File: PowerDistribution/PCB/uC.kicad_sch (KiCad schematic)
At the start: 11 parts, among them IC11 ESP32-S3-WROOM-1U-N8, J10 USB_C_Receptacle_USB2.0_16P, SW1 SW_Push, SW2 SW_Push, U2 USBLC6-2SC6

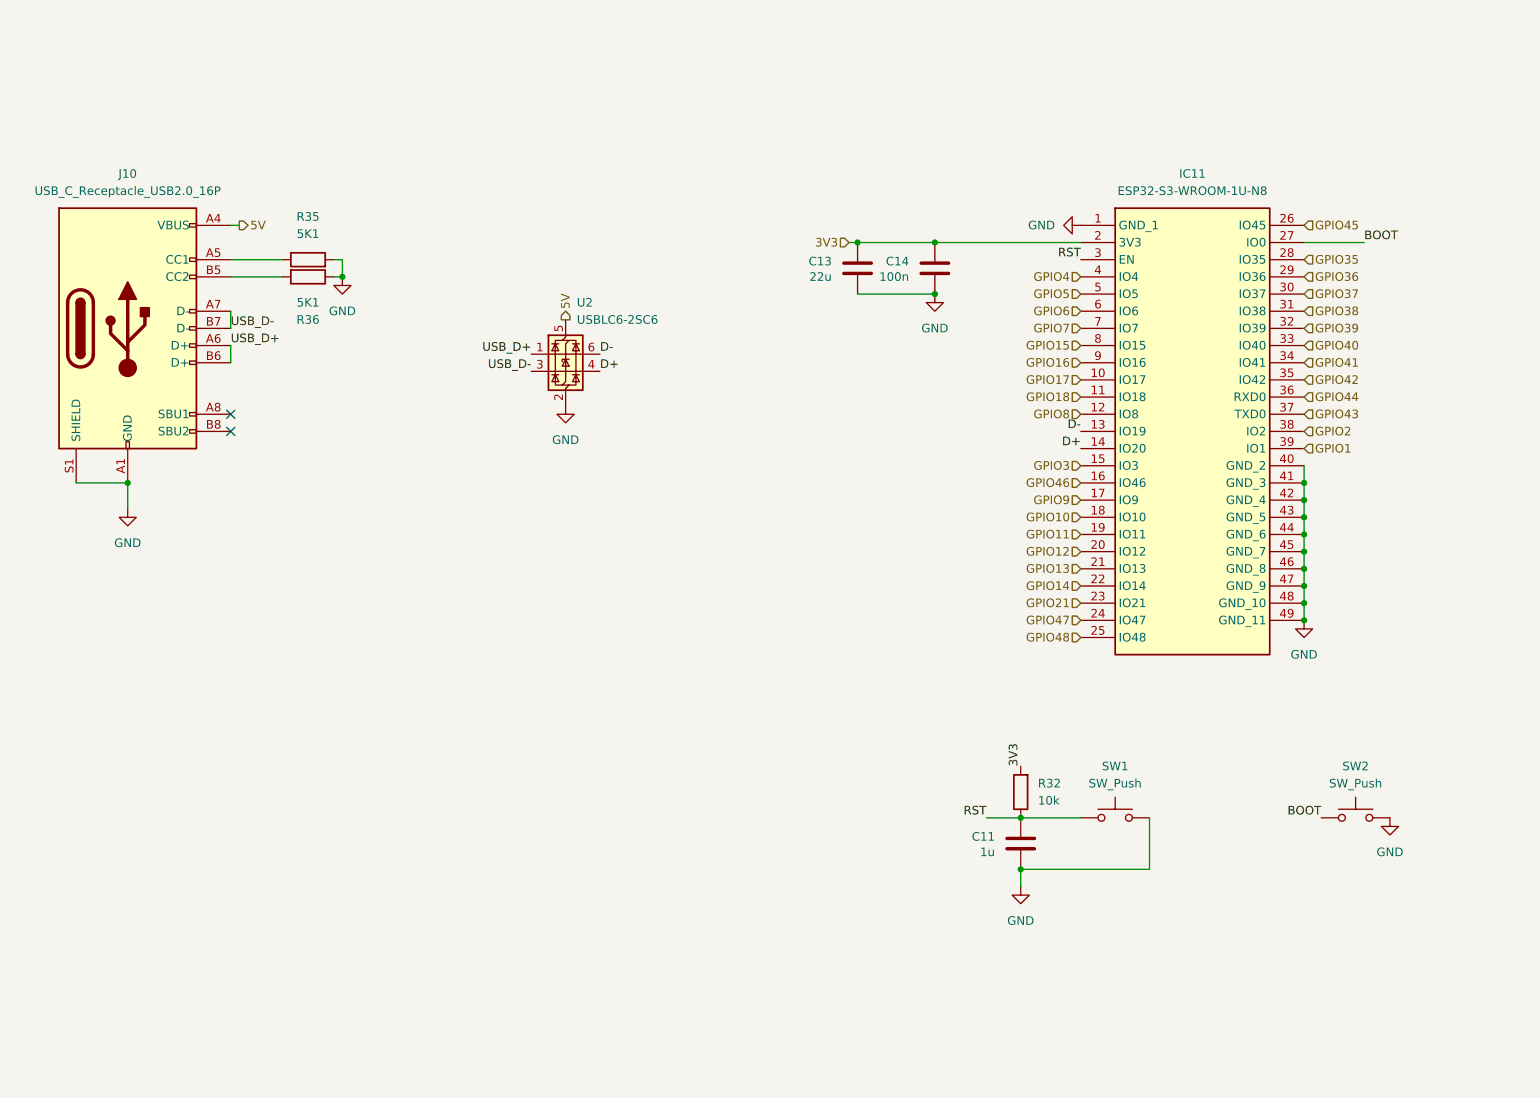
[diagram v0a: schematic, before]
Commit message: Adds PDB v2.0
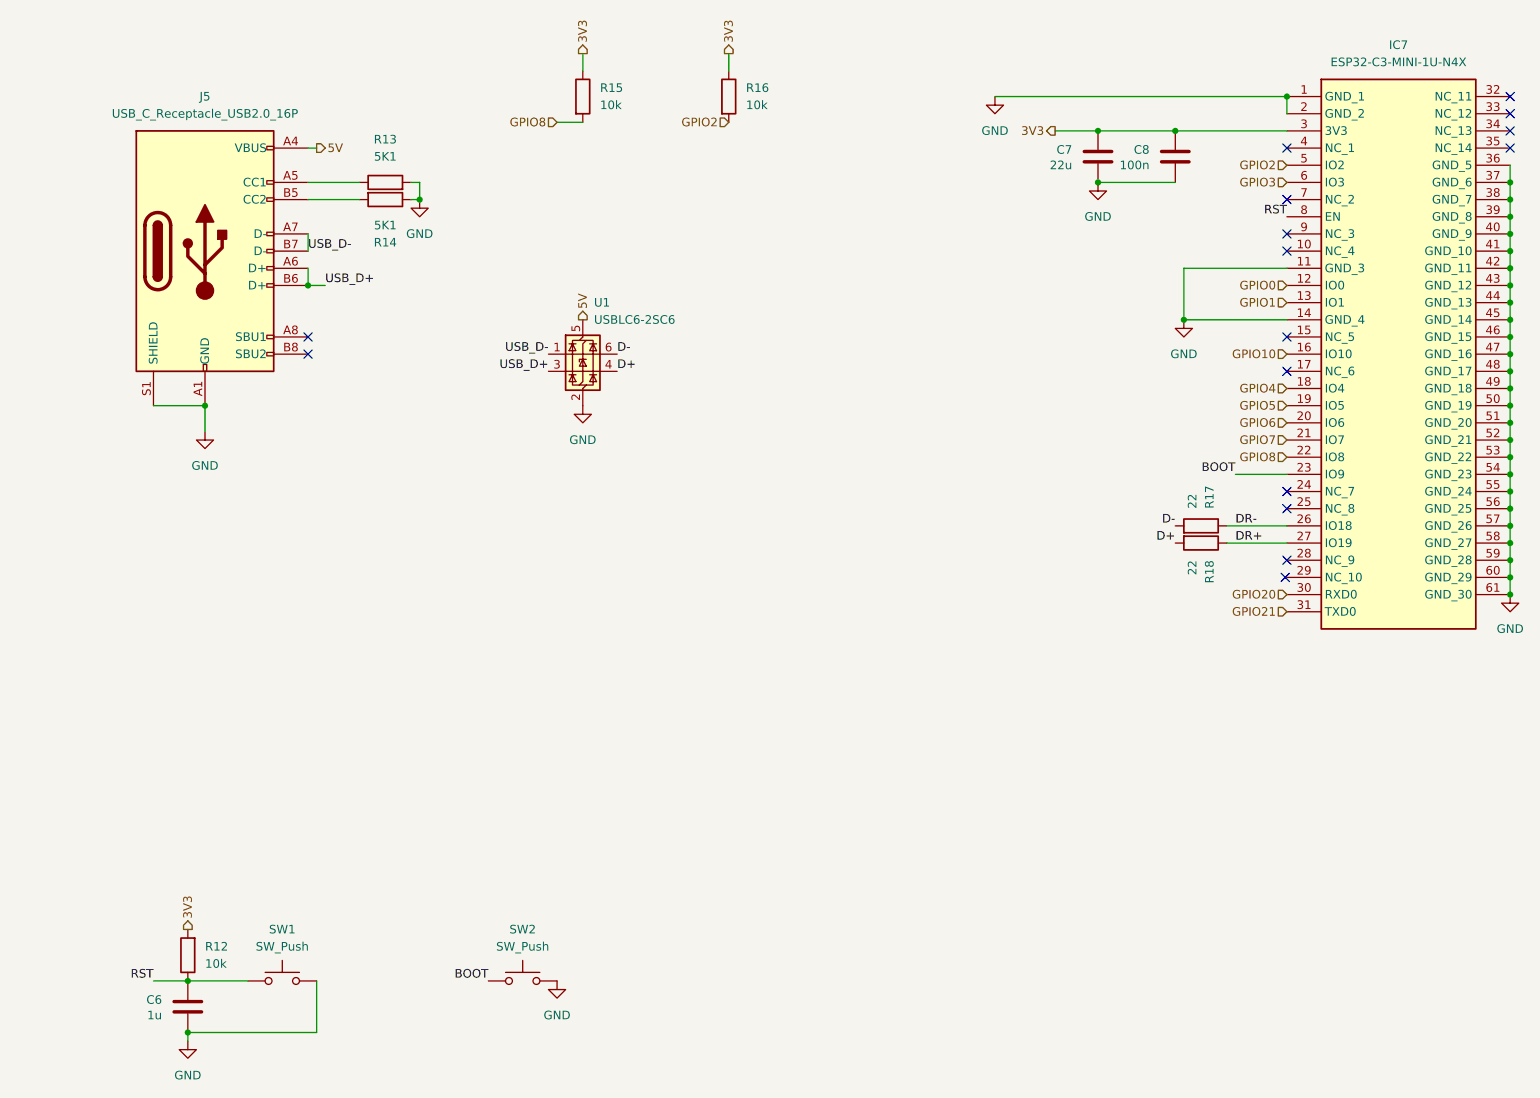
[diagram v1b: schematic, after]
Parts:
- removed C11: 1u, Capacitor_SMD:C_0402_1005Metric, symbol Device:C
- removed C13: 22u, Capacitor_SMD:C_1206_3216Metric, symbol Device:C
- removed C14: 100n, Capacitor_SMD:C_0402_1005Metric, symbol Device:C
- removed IC11: ESP32-S3-WROOM-1U-N8, Footprints:ESP32S3WROOM1UN8, symbol ESP_SMD:ESP32-S3-WROOM-1U-N8
- removed J10: USB_C_Receptacle_USB2.0_16P, Connector_USB:USB_C_Receptacle_G-Switch_GT-USB-7010ASV, symbol Connector:USB_C_Receptacle_USB2.0_16P
- removed R32: 10k, Resistor_SMD:R_0402_1005Metric, symbol Device:R
- removed R35, R36: 5K1, Resistor_SMD:R_0402_1005Metric, symbol Device:R
- removed U2: USBLC6-2SC6, Package_TO_SOT_SMD:SOT-23-6, symbol Power_Protection:USBLC6-2SC6
- added C6: 1u, Capacitor_SMD:C_0402_1005Metric, symbol Device:C
- added C7: 22u, Capacitor_SMD:C_1206_3216Metric, symbol Device:C
- added C8: 100n, Capacitor_SMD:C_0402_1005Metric, symbol Device:C
- added IC7: ESP32-C3-MINI-1U-N4X, ESP32C3MINI1UN4X, symbol ESP_SMD:ESP32-C3-MINI-1U-N4X
- added J5: USB_C_Receptacle_USB2.0_16P, Connector_USB:USB_C_Receptacle_G-Switch_GT-USB-7010ASV, symbol Connector:USB_C_Receptacle_USB2.0_16P
- added R12, R15, R16: 10k, Resistor_SMD:R_0402_1005Metric, symbol Device:R
- added R13, R14: 5K1, Resistor_SMD:R_0402_1005Metric, symbol Device:R
- added R17, R18: 22, Resistor_SMD:R_0402_1005Metric, symbol Device:R
- added U1: USBLC6-2SC6, Package_TO_SOT_SMD:SOT-23-6, symbol Power_Protection:USBLC6-2SC6
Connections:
- net 3V3: now also C7.1, C8.1, IC7.3 (3V3), R12.2, R15.1, R16.1
- net 5V: now also J5.A4 (VBUS), J5.A9 (VBUS), J5.B4 (VBUS), J5.B9 (VBUS), U1.5 (VBUS)
- net BOOT: now also IC7.23 (IO9)
- net D+: now also R18.2, U1.4 (I/O2)
- net D-: now also R17.2, U1.6 (I/O1)
- net GND: now also C6.2, C7.2, C8.2, IC7.1 (GND_1), IC7.11 (GND_3), IC7.14 (GND_4), IC7.2 (GND_2), IC7.36 (GND_5), IC7.37 (GND_6), IC7.38 (GND_7), IC7.39 (GND_8), IC7.40 (GND_9), IC7.41 (GND_10), IC7.42 (GND_11), IC7.43 (GND_12), IC7.44 (GND_13), IC7.45 (GND_14), IC7.46 (GND_15), IC7.47 (GND_16), IC7.48 (GND_17), IC7.49 (GND_18), IC7.50 (GND_19), IC7.51 (GND_20), IC7.52 (GND_21), IC7.53 (GND_22), IC7.54 (GND_23), IC7.55 (GND_24), IC7.56 (GND_25), IC7.57 (GND_26), IC7.58 (GND_27), IC7.59 (GND_28), IC7.60 (GND_29), IC7.61 (GND_30), J5.A1 (GND), J5.A12 (GND), J5.B1 (GND), J5.B12 (GND), J5.S1 (SHIELD), R13.2, R14.1, U1.2 (GND)
- net GPIO1: now also IC7.13 (IO1)
- net GPIO10: now also IC7.16 (IO10)
- net GPIO2: now also IC7.5 (IO2), R16.2
- net GPIO21: now also IC7.31 (TXD0)
- net GPIO3: now also IC7.6 (IO3)
- net GPIO4: now also IC7.18 (IO4)
- net GPIO5: now also IC7.19 (IO5)
- net GPIO6: now also IC7.20 (IO6)
- net GPIO7: now also IC7.21 (IO7)
- net GPIO8: now also IC7.22 (IO8), R15.2
- net RST: now also C6.1, IC7.8 (EN), R12.1
- net USB_D+: now also J5.A6 (D+), J5.B6 (D+), U1.3 (I/O2)
- net USB_D-: now also J5.A7 (D-), J5.B7 (D-), U1.1 (I/O1)
- new net: J5.A5 (CC1), R13.1
- new net: J5.B5 (CC2), R14.2
- new net DR+: IC7.27 (IO19), R18.1
- new net DR-: IC7.26 (IO18), R17.1
- new net GPIO0: IC7.12 (IO0)
- new net GPIO20: IC7.30 (RXD0)
- no-connect marks 2 -> 16
